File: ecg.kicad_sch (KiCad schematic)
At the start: 21 parts, among them SW1 SW_Push, U1 ESP32-S3-PICO-1-N8R2, Y1 Crystal

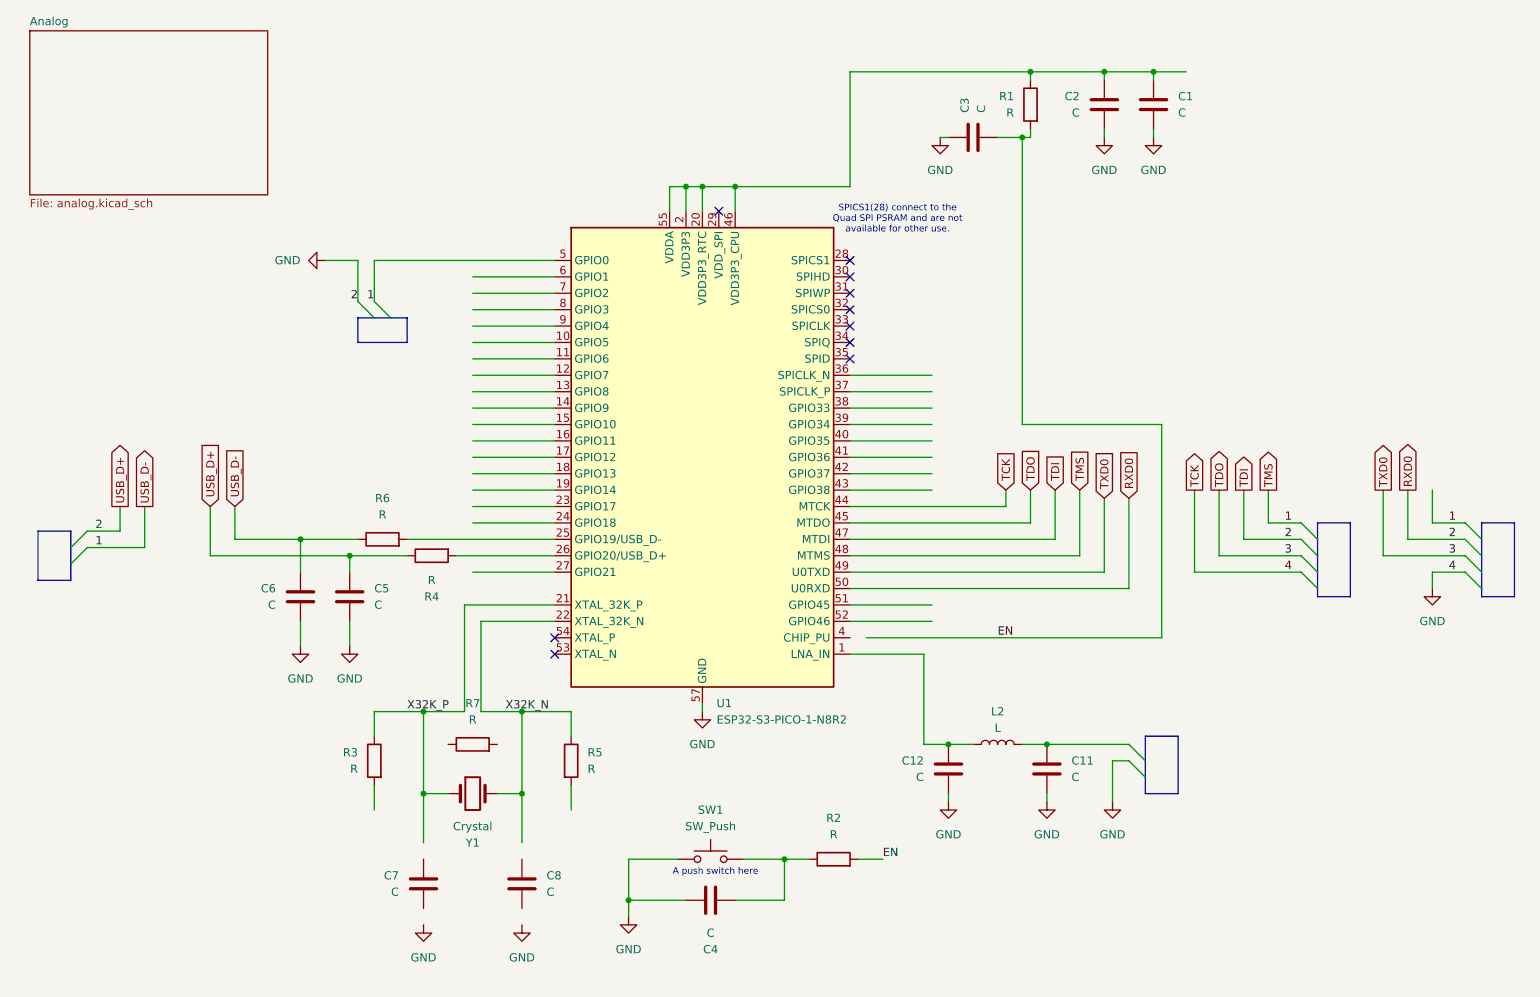
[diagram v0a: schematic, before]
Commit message: removed high pass
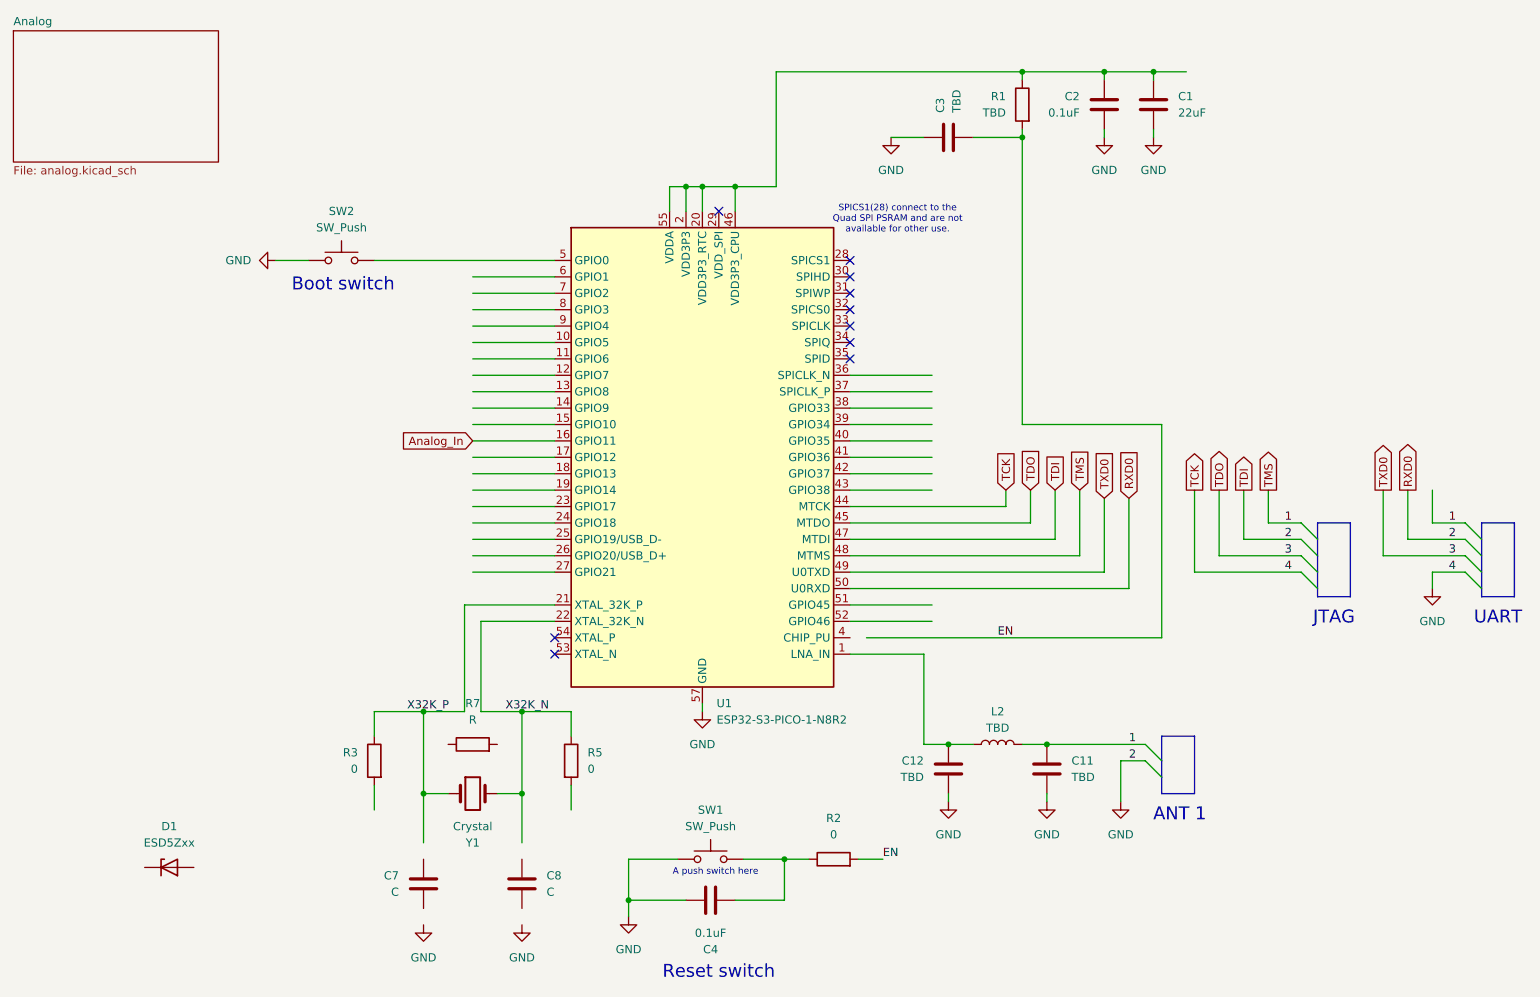
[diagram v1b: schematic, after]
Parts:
- removed C5, C6: C, symbol Device:C
- removed R4, R6: R, symbol Device:R
- added D1: ESD5Zxx, Diode_SMD:D_SOD-523, symbol Diode:ESD5Zxx
- added SW2: SW_Push, symbol Switch:SW_Push
- C1: value C -> 22uF
- C11, C12, C3: value C -> TBD
- C2, C4: value C -> 0.1uF
- L2: value L -> TBD
- R1: value R -> TBD
- R2, R3, R5: value R -> 0
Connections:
- net GND: now also SW2.1
- net TMS: now also C11.1, L2.2; no longer U1.5 (GPIO0)
- net Analog_In: now reaches U1.16 (GPIO11)
- new net: SW2.2, U1.5 (GPIO0)
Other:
- note added: "ANT 1"
- note added: "Boot switch"
- note added: "JTAG"
- note added: "Reset switch"
- note added: "UART"
- title: Wireless ECG(ESDP 2024) -> Wireless ECG
- moved on the sheet: C3, R1

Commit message: Created and added Symbols for previous blackboxes
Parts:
- removed D1: ESD5Zxx, Diode_SMD:D_SOD-523, symbol Diode:ESD5Zxx
- added AN1: ~, symbol antenna_ecg:Antenna_Blackbox
- added JTAG1: ~, symbol jtag:JTAG_Blackbox
- added UART1: ~, symbol uart:UART_Blackbox
- C3: value TBD -> 1uF
- R1: value TBD -> 10k
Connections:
- net GND: now also AN1. (IN), JTAG1. (4), UART1. (GND)
- net TDO: now also JTAG1. (4), UART1. (GND)
- net TMS: now also AN1. (IN), JTAG1. (4), UART1. (GND)
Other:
- note removed: "ANT 1"
- note removed: "JTAG"
- note removed: "UART"

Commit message: Assigned footprints for Resistors and Capacitors
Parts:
- C1, C11, C12, C2, C3, C4, C7, C8: footprint (none) -> Capacitor_SMD:C_0201_0603Metric
- R1, R2, R3, R5, R7: footprint (none) -> Resistor_SMD:R_0201_0603Metric
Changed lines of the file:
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@@
 			)
 		)
-		(property "Footprint" ""
+		(property "Footprint" "Resistor_SMD:R_0201_0603Metric"
 			(at 143.51 146.558 90)
 			(effects
@@
 			)
 		)
-		(property "Footprint" ""
+		(property "Footprint" "Capacitor_SMD:C_0201_0603Metric"
 			(at 192.0748 24.13 0)
 			(effects
@@
 			)
 		)
-		(property "Footprint" ""
+		(property "Footprint" "Resistor_SMD:R_0201_0603Metric"
 			(at 74.168 129.54 90)
 			(effects
@@
 			)
 		)
-		(property "Footprint" ""
+		(property "Footprint" "Resistor_SMD:R_0201_0603Metric"
 			(at 87.63 128.778 90)
 			(effects
@@
 			)
 		)
-		(property "Footprint" ""
+		(property "Footprint" "Capacitor_SMD:C_0201_0603Metric"
 			(at 128.27 150.1648 0)
 			(effects
@@
 			)
 		)
-		(property "Footprint" ""
+		(property "Footprint" "Resistor_SMD:R_0201_0603Metric"
 			(at 101.092 129.54 90)
 			(effects
@@
 			)
 		)
-		(property "Footprint" ""
+		(property "Footprint" "Capacitor_SMD:C_0201_0603Metric"
 			(at 186.3852 24.13 0)
 			(effects
@@
 			)
 		)
-		(property "Footprint" ""
+		(property "Footprint" "Capacitor_SMD:C_0201_0603Metric"
 			(at 160.3248 134.62 0)
 			(effects
@@
 			)
 		)
-		(property "Footprint" ""
+		(property "Footprint" "Capacitor_SMD:C_0201_0603Metric"
 			(at 177.4952 134.62 0)
 			(effects
@@
 			)
 		)
-		(property "Footprint" ""
+		(property "Footprint" "Resistor_SMD:R_0201_0603Metric"
 			(at 174.498 27.94 90)
 			(effects
@@
 			)
 		)
-		(property "Footprint" ""
+		(property "Footprint" "Capacitor_SMD:C_0201_0603Metric"
 			(at 96.2152 152.4 0)
 			(effects
@@
 			)
 		)
-		(property "Footprint" ""
+		(property "Footprint" "Capacitor_SMD:C_0201_0603Metric"
 			(at 157.48 33.9852 0)
 			(effects
@@
 			)
 		)
-		(property "Footprint" ""
+		(property "Footprint" "Capacitor_SMD:C_0201_0603Metric"
 			(at 79.0448 152.4 0)
 			(effects
@@
 	)
 	(sheet
-		(at 16.51 16.51)
+		(at 17.78 17.78)
 		(size 31.75 20.32)
 		(fields_autoplaced yes)
@@
 		)
 		(property "Sheetname" "Analog"
-			(at 16.51 15.7984 0)
+			(at 17.78 17.0684 0)
 			(effects
 				(font
@@
 		)
 		(property "Sheetfile" "analog.kicad_sch"
-			(at 16.51 37.4146 0)
-			(effects
-				(font
+			(at 17.78 38.6846 0)
+			(effects
+				(font

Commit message: Connected external oscillator
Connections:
- net GND: now also C7.2, C8.2
- net X32K_N: now also C8.1, R7.2
- net X32K_P: now also C7.1, R7.1
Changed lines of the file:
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@@
+	)
+	(junction
+		(at 80.01 127)
+		(diameter 0)
+		(color 0 0 0 0)
 	)
 	(junction
@@
 	(junction
 		(at 111.76 151.13)
+		(diameter 0)
+		(color 0 0 0 0)
+	)
+	(junction
+		(at 95.25 127)
 		(diameter 0)
 		(color 0 0 0 0)
@@
 	(wire
 		(pts
-			(xy 80.01 134.62) (xy 80.01 142.24)
-		)
-		(stroke
-			(width 0)
-			(type default)
-		)
-	)
-	(wire
-		(pts
-			(xy 80.01 121.92) (xy 80.01 134.62)
+			(xy 80.01 134.62) (xy 80.01 144.78)
+		)
+		(stroke
+			(width 0)
+			(type default)
+		)
+	)
+	(wire
+		(pts
+			(xy 80.01 121.92) (xy 80.01 127)
 		)
 		(stroke
@@
 	(wire
 		(pts
+			(xy 95.25 152.4) (xy 95.25 154.94)
+		)
+		(stroke
+			(width 0)
+			(type default)
+		)
+	)
+	(wire
+		(pts
 			(xy 146.05 95.25) (xy 177.8 95.25)
 		)
@@
 	(wire
 		(pts
-			(xy 95.25 121.92) (xy 95.25 134.62)
+			(xy 95.25 121.92) (xy 95.25 127)
 		)
 		(stroke
@@
 	(wire
 		(pts
+			(xy 91.44 127) (xy 95.25 127)
+		)
+		(stroke
+			(width 0)
+			(type default)
+		)
+	)
+	(wire
+		(pts
 			(xy 87.63 67.31) (xy 100.33 67.31)
 		)
@@
 	(wire
 		(pts
-			(xy 95.25 142.24) (xy 95.25 134.62)
+			(xy 95.25 134.62) (xy 95.25 144.78)
 		)
 		(stroke
@@
 	(wire
 		(pts
+			(xy 80.01 152.4) (xy 80.01 154.94)
+		)
+		(stroke
+			(width 0)
+			(type default)
+		)
+	)
+	(wire
+		(pts
 			(xy 157.48 113.03) (xy 157.48 127)
 		)
@@
 	(wire
 		(pts
+			(xy 95.25 127) (xy 95.25 134.62)
+		)
+		(stroke
+			(width 0)
+			(type default)
+		)
+	)
+	(wire
+		(pts
 			(xy 87.63 77.47) (xy 100.33 77.47)
 		)
@@
 	(wire
 		(pts
+			(xy 80.01 127) (xy 80.01 134.62)
+		)
+		(stroke
+			(width 0)
+			(type default)
+		)
+	)
+	(wire
+		(pts
 			(xy 194.31 77.47) (xy 194.31 110.49)
 		)
@@
 		)
 		(stroke
+			(width 0)
+			(type default)
+		)
+	)
+	(wire
+		(pts
+			(xy 80.01 127) (xy 83.82 127)
+		)
+		(stroke

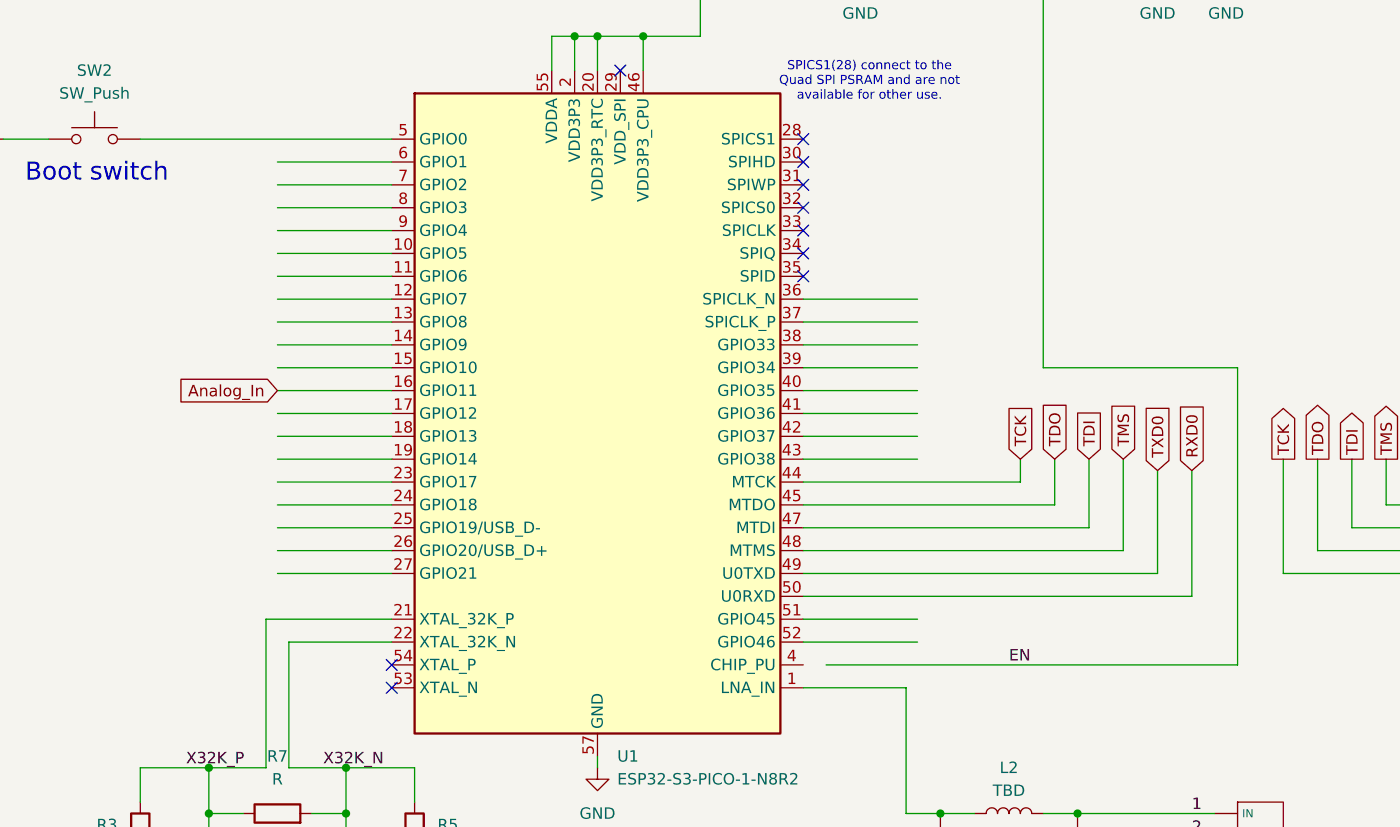
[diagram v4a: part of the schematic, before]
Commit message: Connect unused GPIO pins to Vs-
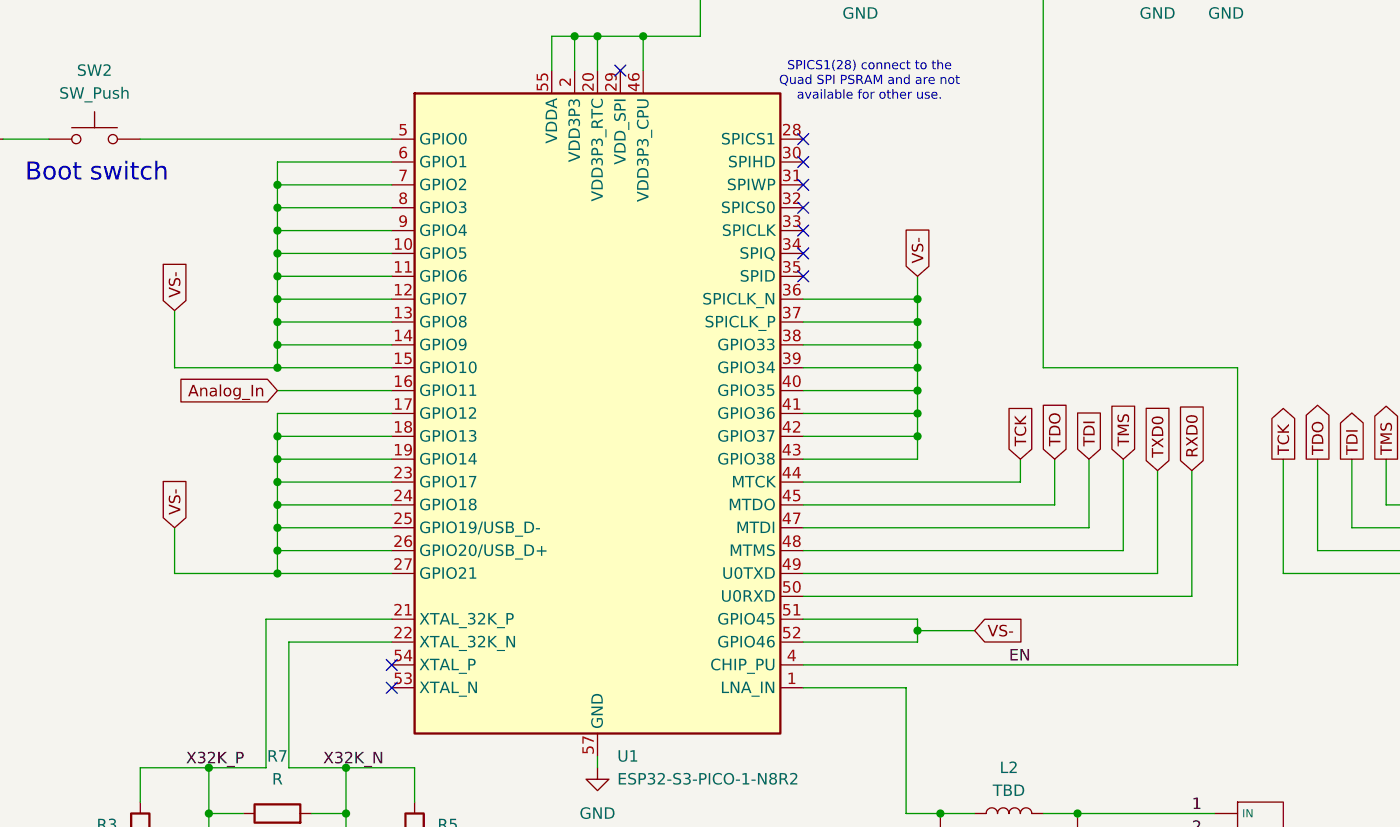
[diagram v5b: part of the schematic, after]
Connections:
- net EN: now also U1.4 (CHIP_PU)
- net VS-: now reaches U1.10 (GPIO5)
- net VS-: now also U1.11 (GPIO6), U1.12 (GPIO7), U1.13 (GPIO8), U1.14 (GPIO9), U1.15 (GPIO10), U1.17 (GPIO12), U1.18 (GPIO13), U1.19 (GPIO14), U1.23 (GPIO17), U1.24 (GPIO18), U1.25 (GPIO19/USB_D-), U1.26 (GPIO20/USB_D+), U1.27 (GPIO21), U1.36 (SPICLK_N), U1.37 (SPICLK_P), U1.38 (GPIO33), U1.39 (GPIO34), U1.40 (GPIO35), U1.41 (GPIO36), U1.42 (GPIO37), U1.43 (GPIO38), U1.51 (GPIO45), U1.52 (GPIO46), U1.6 (GPIO1), U1.7 (GPIO2), U1.8 (GPIO3), U1.9 (GPIO4)
